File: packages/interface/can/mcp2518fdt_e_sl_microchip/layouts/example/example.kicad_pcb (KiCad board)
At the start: 2 copper layers, 6 parts

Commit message: Make package builds deterministic by wiring explicit local parts
The remaining packages now reference package-local concrete passives,
inductors, and other small parts directly instead of relying on generic
part-picker resolution. This aligns the source with the local
assets and removes the flaky live EasyEDA lookup path that was blocking
verification.

Constraint: Builds must not depend on unstable live part-picking when local package assets already exist
Constraint: Package-local parts remain the ownership boundary; no shared global part store was introduced
Rejected: Keep generic passives as the default style | repeated verification failures from upstream EasyEDA API instability
Rejected: Add ad hoc offline hacks around ato part-picking | weaker than making the package source deterministic
Confidence: high
Scope-risk: moderate
Reversibility: clean
Directive: For packages that already own generated local parts, instantiate those part modules directly and avoid generic passive declarations unless there is a strong reason not to
Tested:  passed for stm32g0b1kbu6_st, mcp2518fdt_e_sl_microchip, tcan3413ddfr_ti, raspberry_pi_hat_socket_zhouri, bq40z50rsmr_r2_4s_3a_ti, tps56637rpar_5v1_5a_ti, tps62933drlr_3v3_ti, bq25756rrvr_4s_2a_ti, tps2121ruxr_20v_4a_ti, and tps25730drefr_20v_3a_ti
Not-tested: Cross-package downstream integration beyond each package's default/example build
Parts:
- C1, C2: value 15pF ±5% -> (none)
- C3: value 1µF ±10% -> (none)
- C4: value 100nF ±10% -> (none)
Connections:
- net osc1_load-power-hv renamed can_ctrl-1
- net osc2_load-power-hv renamed 1
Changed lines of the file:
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@@
 	(net 7 "CLKO_SOF")
 	(net 8 "nINT")
-	(net 9 "osc1_load-power-hv")
+	(net 9 "can_ctrl-1")
 	(net 10 "8")
 	(net 11 "nINT0_GPIO0_XSTBY")
-	(net 12 "osc2_load-power-hv")
+	(net 12 "1")
 	(net 13 "lv")
 	(net 14 "hv")
@@
 			(size 0.57 2.04)
 			(layers "F.Cu" "F.Paste" "F.Mask")
-			(net 9 "osc1_load-power-hv")
+			(net 9 "can_ctrl-1")
 		)
 		(pad "5" smd oval
@@
 			(size 0.57 2.04)
 			(layers "F.Cu" "F.Paste" "F.Mask")
-			(net 12 "osc2_load-power-hv")
+			(net 12 "1")
 		)
 		(pad "4" smd oval
@@
 			(size 0.9 0.8)
 			(layers "F.Cu" "F.Paste" "F.Mask")
-			(net 12 "osc2_load-power-hv")
+			(net 12 "1")
 		)
 		(pad "4" smd rect
@@
 			(size 0.9 0.8)
 			(layers "F.Cu" "F.Paste" "F.Mask")
-			(net 9 "osc1_load-power-hv")
+			(net 9 "can_ctrl-1")
 		)
 		(embedded_fonts no)
@@
 			)
 		)
-		(property "Value" "15pF ±5%"
+		(property "Value" ""
 			(at 0 4)
 			(layer "F.Fab")
@@
 			(hide yes)
 		)
-		(property "Datasheet" "https://www.lcsc.com/datasheet/lcsc_datasheet_1810011652_Murata-Electronics-GRM1555C1H150JA01D_C76950.pdf"
+		(property "Datasheet" "https://www.lcsc.com/datasheet/lcsc_datasheet_1811081611_Murata-Electronics-GRM1555C1H150JA01D_C76950.pdf"
 			(at 0 0 0)
 			(layer "User.9")
@@
 			(size 0.5 0.54)
 			(layers "F.Cu" "F.Paste" "F.Mask")
-			(net 9 "osc1_load-power-hv")
+			(net 9 "can_ctrl-1")
 		)
 		(embedded_fonts no)
@@
 			)
 		)
-		(property "Value" "15pF ±5%"
+		(property "Value" ""
 			(at 0 4)
 			(layer "F.Fab")
@@
 			(hide yes)
 		)
-		(property "Datasheet" "https://www.lcsc.com/datasheet/lcsc_datasheet_1810011652_Murata-Electronics-GRM1555C1H150JA01D_C76950.pdf"
+		(property "Datasheet" "https://www.lcsc.com/datasheet/lcsc_datasheet_1811081611_Murata-Electronics-GRM1555C1H150JA01D_C76950.pdf"
 			(at 0 0 0)
 			(layer "User.9")
@@
 			(size 0.5 0.54)
 			(layers "F.Cu" "F.Paste" "F.Mask")
-			(net 12 "osc2_load-power-hv")
+			(net 12 "1")
 		)
 		(embedded_fonts no)
@@
 			)
 		)
-		(property "Value" "1µF ±10%"
+		(property "Value" ""
 			(at 0 4)
 			(layer "F.Fab")
@@
 			(hide yes)
 		)
-		(property "Datasheet" "https://www.lcsc.com/datasheet/lcsc_datasheet_1810011711_Murata-Electronics-GRM155R61C105KE01D_C77007.pdf"
+		(property "Datasheet" "https://wmsc.lcsc.com/wmsc/upload/file/pdf/v2/lcsc/1811081724_Murata-Electronics-GRM155R61C105KE01D_C77007.pdf"
 			(at 0 0 0)
 			(layer "User.9")
@@
 			)
 		)
-		(property "Value" "100nF ±10%"
+		(property "Value" ""
 			(at 0 4)
 			(layer "F.Fab")

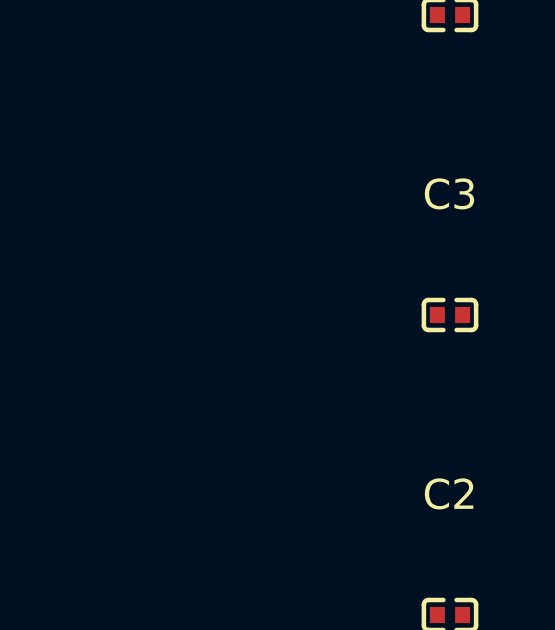
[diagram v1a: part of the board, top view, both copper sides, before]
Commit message: Make package schematics more readable and align passive choices with repo guidance
This pass improves the human-facing quality of the package library.
Explicit local capacitor/resistor parts now carry short descriptive
comments at the point of use, the MCP2518FD package swaps its 1uF bulk
capacitor to a 0603 part to match the current sizing rule, and several
packages add better net-name overrides for exposed and important internal
signals.

Constraint: Repo guidance now prefers explicit local parts and expects readable schematic net names
Constraint: Passive sizing should follow the current MLCC package rule unless a justified exception is needed
Rejected: Keep part instances comment-free | explicit local part names are not readable enough by themselves
Rejected: Leave the MCP2518FD 1uF bulk cap in 0402 | conflicts with the current 1uF-10uF 0603 guidance
Confidence: medium
Scope-risk: moderate
Reversibility: clean
Directive: When instantiating explicit local resistor/capacitor parts, include a short readable comment with the key value/package characteristics unless the name is already obviously human-readable
Tested:  passed for stm32g0b1kbu6_st, mcp2518fdt_e_sl_microchip, tcan3413ddfr_ti, raspberry_pi_hat_socket_zhouri, bq40z50rsmr_r2_4s_3a_ti, tps56637rpar_5v1_5a_ti, tps62933drlr_3v3_ti, bq25756rrvr_4s_2a_ti, tps2121ruxr_20v_4a_ti, and tps25730drefr_20v_3a_ti
Not-tested: Complete elimination of all internal autogenerated net labels in every package; some deep internal nets may still remain tool-driven
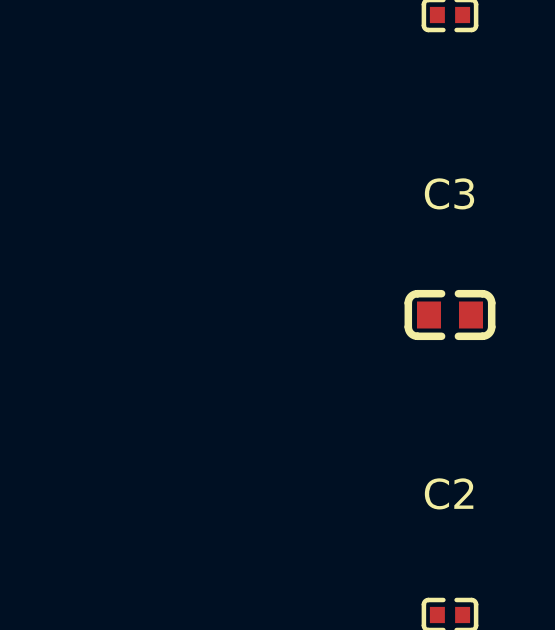
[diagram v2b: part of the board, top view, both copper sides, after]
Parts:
- C3: footprint Murata_Electronics_GRM155R61C105KE01D:C0402 -> Murata_Electronics_GRM188R61H105KAALD:C0603
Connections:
- net 1 renamed OSC2
- net 8 renamed nINT1_GPIO1
- net can_ctrl-1 renamed OSC1
- net hv renamed +3.3V
- net lv renamed GND
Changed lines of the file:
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@@
 	(net 7 "CLKO_SOF")
 	(net 8 "nINT")
-	(net 9 "can_ctrl-1")
-	(net 10 "8")
+	(net 9 "OSC1")
+	(net 10 "nINT1_GPIO1")
 	(net 11 "nINT0_GPIO0_XSTBY")
-	(net 12 "1")
-	(net 13 "lv")
-	(net 14 "hv")
+	(net 12 "OSC2")
+	(net 13 "GND")
+	(net 14 "+3.3V")
 	(footprint "Microchip_Tech_MCP2518FDT_E_SL:SOIC-14_L8.7-W3.9-P1.27-LS6.0-BL"
 		(layer "F.Cu")
@@
 			(size 0.57 2.04)
 			(layers "F.Cu" "F.Paste" "F.Mask")
-			(net 10 "8")
+			(net 10 "nINT1_GPIO1")
 		)
 		(pad "9" smd oval
@@
 			(size 0.57 2.04)
 			(layers "F.Cu" "F.Paste" "F.Mask")
-			(net 14 "hv")
+			(net 14 "+3.3V")
 		)
 		(pad "7" smd oval
@@
 			(size 0.57 2.04)
 			(layers "F.Cu" "F.Paste" "F.Mask")
-			(net 13 "lv")
+			(net 13 "GND")
 		)
 		(pad "6" smd oval
@@
 			(size 0.57 2.04)
 			(layers "F.Cu" "F.Paste" "F.Mask")
-			(net 9 "can_ctrl-1")
+			(net 9 "OSC1")
 		)
 		(pad "5" smd oval
@@
 			(size 0.57 2.04)
 			(layers "F.Cu" "F.Paste" "F.Mask")
-			(net 12 "1")
+			(net 12 "OSC2")
 		)
 		(pad "4" smd oval
@@
 			(size 0.9 0.8)
 			(layers "F.Cu" "F.Paste" "F.Mask")
-			(net 13 "lv")
+			(net 13 "GND")
 		)
 		(pad "3" smd rect
@@
 			(size 0.9 0.8)
 			(layers "F.Cu" "F.Paste" "F.Mask")
-			(net 12 "1")
+			(net 12 "OSC2")
 		)
 		(pad "4" smd rect
@@
 			(size 0.9 0.8)
 			(layers "F.Cu" "F.Paste" "F.Mask")
-			(net 13 "lv")
+			(net 13 "GND")
 		)
 		(pad "1" smd rect
@@
 			(size 0.9 0.8)
 			(layers "F.Cu" "F.Paste" "F.Mask")
-			(net 9 "can_ctrl-1")
+			(net 9 "OSC1")
 		)
 		(embedded_fonts no)
@@
 			(size 0.5 0.54)
 			(layers "F.Cu" "F.Paste" "F.Mask")
-			(net 13 "lv")
+			(net 13 "GND")
 		)
 		(pad "1" smd rect
@@
 			(size 0.5 0.54)
 			(layers "F.Cu" "F.Paste" "F.Mask")
-			(net 9 "can_ctrl-1")
+			(net 9 "OSC1")
 		)
 		(embedded_fonts no)
@@
 			(size 0.5 0.54)
 			(layers "F.Cu" "F.Paste" "F.Mask")
-			(net 13 "lv")
+			(net 13 "GND")
 		)
 		(pad "1" smd rect
@@
 			(size 0.5 0.54)
 			(layers "F.Cu" "F.Paste" "F.Mask")
-			(net 12 "1")
+			(net 12 "OSC2")
 		)
 		(embedded_fonts no)
@@
 		)
 	)
-	(footprint "Murata_Electronics_GRM155R61C105KE01D:C0402"
+	(footprint "Murata_Electronics_GRM188R61H105KAALD:C0603"
 		(layer "F.Cu")
 		(at 20 -20 0)
@@
 			)
 		)
-		(property "LCSC" "C77007"
+		(property "LCSC" "C77386"
 			(at 0 0 0)
 			(layer "User.9")
@@
 			(hide yes)
 		)
-		(property "Partnumber" "GRM155R61C105KE01D"
-			(at 0 0 0)
-			(layer "User.9")
-			(hide yes)
-		)
-		(property "Datasheet" "https://wmsc.lcsc.com/wmsc/upload/file/pdf/v2/lcsc/1811081724_Murata-Electronics-GRM155R61C105KE01D_C77007.pdf"
+		(property "Partnumber" "GRM188R61H105KAALD"
+			(at 0 0 0)
+			(layer "User.9")
+			(hide yes)
+		)
+		(property "Datasheet" "https://wmsc.lcsc.com/wmsc/upload/file/pdf/v2/lcsc/1811012005_Murata-Electronics-GRM188R61H105KAALD_C77386.pdf"
 			(at 0 0 0)
 			(layer "User.9")
@@
 			(hide yes)
 		)
-		(property "lcsc_id" "C77007"
+		(property "lcsc_id" "C77386"
 			(at 0 0 0)
 			(layer "User.9")
@@
 		(attr smd)
 		(fp_line
-			(start -0.72 -0.5)
-			(end -0.22 -0.5)
-			(stroke
-				(width 0.15)
-				(type solid)
-			)
-			(layer "F.SilkS")
-			(layers "F.SilkS")
-			(locked no)
-		)
-		(fp_line
-			(start -0.87 0.35)
-			(end -0.87 -0.35)
-			(stroke
-				(width 0.15)
-				(type solid)
-			)
-			(layer "F.SilkS")
-			(layers "F.SilkS")
-			(locked no)
-		)
-		(fp_line
-			(start -0.22 0.5)
-			(end -0.72 0.5)
-			(stroke
-				(width 0.15)
-				(type solid)
-			)
-			(layer "F.SilkS")
-			(layers "F.SilkS")
-			(locked no)
-		)
-		(fp_line
-			(start 0.72 0.5)
-			(end 0.22 0.5)
-			(stroke
-				(width 0.15)
-				(type solid)
-			)
-			(layer "F.SilkS")
-			(layers "F.SilkS")
-			(locked no)
-		)
-		(fp_line
-			(start 0.22 -0.5)
-			(end 0.72 -0.5)
-			(stroke
-				(width 0.15)
-				(type solid)
-			)
-			(layer "F.SilkS")
-			(layers "F.SilkS")
-			(locked no)
-		)
-		(fp_line
-			(start 0.87 -0.35)
-			(end 0.87 0.35)
-			(stroke
-				(width 0.15)
-				(type solid)
-			)
-			(layer "F.SilkS")
-			(layers "F.SilkS")
-			(locked no)
-		)
-		(fp_arc
-			(start 0.87 -0.35)
-			(mid 0.826066 -0.456066)
-			(end 0.72 -0.5)
-			(stroke
-				(width 0.15)
-				(type solid)
-			)
-			(layer "F.SilkS")
-			(locked no)
-		)
-		(fp_arc
-			(start 0.72 0.5)
-			(mid 0.826066 0.456066)
-			(end 0.87 0.35)
-			(stroke
-				(width 0.15)
-				(type solid)
-			)
-			(layer "F.SilkS")
-			(locked no)
-		)
-		(fp_arc
-			(start -0.87 0.35)
-			(mid -0.826066 0.456066)
-			(end -0.72 0.5)
-			(stroke
-				(width 0.15)
-				(type solid)
-			)
-			(layer "F.SilkS")
-			(locked no)
-		)
-		(fp_arc
-			(start -0.72 -0.5)
-			(mid -0.826066 -0.456066)
-			(end -0.87 -0.35)
-			(stroke
-				(width 0.15)
+			(start -0.28 0.71)
+			(end -1.08 0.71)
+			(stroke
+				(width 0.25)
+				(type solid)
+			)
+			(layer "F.SilkS")
+			(layers "F.SilkS")
+			(locked no)
+		)
+		(fp_line
+			(start 0.28 0.71)
+			(end 1.08 0.71)
+			(stroke
+				(width 0.25)
+				(type solid)
+			)
+			(layer "F.SilkS")
+			(layers "F.SilkS")
+			(locked no)
+		)
+		(fp_line
+			(start -0.28 -0.71)
+			(end -1.08 -0.71)
+			(stroke
+				(width 0.25)
+				(type solid)
+			)
+			(layer "F.SilkS")
+			(layers "F.SilkS")
+			(locked no)
+		)
+		(fp_line
+			(start 0.28 -0.71)
+			(end 1.08 -0.71)
+			(stroke
+				(width 0.25)
+				(type solid)
+			)
+			(layer "F.SilkS")
+			(layers "F.SilkS")
+			(locked no)
+		)
+		(fp_line
+			(start -1.39 0.4)
+			(end -1.39 -0.4)
+			(stroke
+				(width 0.25)
+				(type solid)
+			)
+			(layer "F.SilkS")
+			(layers "F.SilkS")
+			(locked no)
+		)
+		(fp_line
+			(start 1.39 -0.4)
+			(end 1.39 0.4)
+			(stroke
+				(width 0.25)
+				(type solid)
+			)
+			(layer "F.SilkS")
+			(layers "F.SilkS")
+			(locked no)
+		)
+		(fp_arc
+			(start 1.39 -0.4)
+			(mid 1.2992031 -0.6192031)
+			(end 1.08 -0.71)
+			(stroke
+				(width 0.25)
+				(type solid)
+			)
+			(layer "F.SilkS")
+			(locked no)
+		)
+		(fp_arc
+			(start 1.08 0.71)
+			(mid 1.2992031 0.6192031)
+			(end 1.39 0.4)
+			(stroke
+				(width 0.25)
+				(type solid)
+			)
+			(layer "F.SilkS")
+			(locked no)
+		)
+		(fp_arc
+			(start -1.39 0.4)
+			(mid -1.2992031 0.6192031)
+			(end -1.08 0.71)
+			(stroke
+				(width 0.25)
+				(type solid)
+			)
+			(layer "F.SilkS")
+			(locked no)
+		)
+		(fp_arc
+			(start -1.08 -0.71)
+			(mid -1.2992031 -0.6192031)
+			(end -1.39 -0.4)
+			(stroke
+				(width 0.25)
 				(type solid)
 			)
@@
 		)
 		(fp_circle
-			(center -0.5 0.25)
-			(end -0.47 0.25)
+			(center -0.8 0.4)
+			(end -0.77 0.4)
 			(stroke
 				(width 0.06)
@@
 		)
 		(pad "2" smd rect
-			(at 0.42 0 0)
-			(size 0.5 0.54)
-			(layers "F.Cu" "F.Paste" "F.Mask")
-			(net 13 "lv")
+			(at 0.7 0 0)
+			(size 0.8 0.9)
+			(layers "F.Cu" "F.Paste" "F.Mask")
+			(net 13 "GND")
 		)
 		(pad "1" smd rect
-			(at -0.42 0 0)
-			(size 0.5 0.54)
-			(layers "F.Cu" "F.Paste" "F.Mask")
-			(net 14 "hv")
+			(at -0.7 0 0)
+			(size 0.8 0.9)
+			(layers "F.Cu" "F.Paste" "F.Mask")
+			(net 14 "+3.3V")
 		)
 		(embedded_fonts no)
-		(model "${KIPRJMOD}/../../parts/Murata_Electronics_GRM155R61C105KE01D/C0402_L1.0-W0.5-H0.5.step"
+		(model "${KIPRJMOD}/../../parts/Murata_Electronics_GRM188R61H105KAALD/C0603_L1.6-W0.8-H0.8.step"
 			(offset
 				(xyz 0 0 -0)
@@
 			(size 0.5 0.54)
 			(layers "F.Cu" "F.Paste" "F.Mask")
-			(net 13 "lv")
+			(net 13 "GND")
 		)
 		(pad "1" smd rect
@@
 			(size 0.5 0.54)
 			(layers "F.Cu" "F.Paste" "F.Mask")
-			(net 14 "hv")
+			(net 14 "+3.3V")
 		)
 		(embedded_fonts no)

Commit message: Finish removing net-name overrides from reusable packages
This completes the package-level override cleanup by deleting the remaining
`override_net_name` assignments from the library's reusable package modules and
rebuilding their checked-in layouts so generated net metadata matches source.
The package interfaces stay the same; only the forced net naming was removed so
these modules compose cleanly when imported into downstream designs.

Constraint: The library must stay reusable and avoid imposed internal net names leaking into consuming designs
Constraint: Each changed package must still verify with the repo's Atopile workflow after layout regeneration
Rejected: Stop after the battery frontend cleanup | leaves the same composition hazard in other packages
Rejected: Remove override lines without rebuilding layouts | would leave stale generated PCB net names checked into the repo
Confidence: high
Scope-risk: moderate
Reversibility: clean
Directive: Do not reintroduce `override_net_name` in reusable package modules unless a package is intentionally design-specific
Tested: `uv tool run --from atopile==0.15.4 ato --non-interactive build` in each affected package directory (stm32g0b1kbu6_st, mcp2518fdt_e_sl_microchip, tcan3413ddfr_ti, raspberry_pi_hat_socket_zhouri, tps56637rpar_5v1_5a_ti, tps62933drlr_3v3_ti, bq25756rrvr_4s_2a_ti, tps2121ruxr_20v_4a_ti, tps25730drefr_20v_3a_ti)
Not-tested: Downstream consumer projects that may have been depending on the old forced net names in generated layouts
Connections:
- net +3.3V renamed hv
- net GND renamed lv
- net OSC1 renamed can_ctrl-1
- net OSC2 renamed 1
- net nINT1_GPIO1 renamed 8
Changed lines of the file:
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@@
 	(net 7 "CLKO_SOF")
 	(net 8 "nINT")
-	(net 9 "OSC1")
-	(net 10 "nINT1_GPIO1")
+	(net 9 "can_ctrl-1")
+	(net 10 "8")
 	(net 11 "nINT0_GPIO0_XSTBY")
-	(net 12 "OSC2")
-	(net 13 "GND")
-	(net 14 "+3.3V")
+	(net 12 "1")
+	(net 13 "lv")
+	(net 14 "hv")
 	(footprint "Microchip_Tech_MCP2518FDT_E_SL:SOIC-14_L8.7-W3.9-P1.27-LS6.0-BL"
 		(layer "F.Cu")
@@
 			(size 0.57 2.04)
 			(layers "F.Cu" "F.Paste" "F.Mask")
-			(net 10 "nINT1_GPIO1")
+			(net 10 "8")
 		)
 		(pad "9" smd oval
@@
 			(size 0.57 2.04)
 			(layers "F.Cu" "F.Paste" "F.Mask")
-			(net 14 "+3.3V")
+			(net 14 "hv")
 		)
 		(pad "7" smd oval
@@
 			(size 0.57 2.04)
 			(layers "F.Cu" "F.Paste" "F.Mask")
-			(net 13 "GND")
+			(net 13 "lv")
 		)
 		(pad "6" smd oval
@@
 			(size 0.57 2.04)
 			(layers "F.Cu" "F.Paste" "F.Mask")
-			(net 9 "OSC1")
+			(net 9 "can_ctrl-1")
 		)
 		(pad "5" smd oval
@@
 			(size 0.57 2.04)
 			(layers "F.Cu" "F.Paste" "F.Mask")
-			(net 12 "OSC2")
+			(net 12 "1")
 		)
 		(pad "4" smd oval
@@
 			(size 0.9 0.8)
 			(layers "F.Cu" "F.Paste" "F.Mask")
-			(net 13 "GND")
+			(net 13 "lv")
 		)
 		(pad "3" smd rect
@@
 			(size 0.9 0.8)
 			(layers "F.Cu" "F.Paste" "F.Mask")
-			(net 12 "OSC2")
+			(net 12 "1")
 		)
 		(pad "4" smd rect
@@
 			(size 0.9 0.8)
 			(layers "F.Cu" "F.Paste" "F.Mask")
-			(net 13 "GND")
+			(net 13 "lv")
 		)
 		(pad "1" smd rect
@@
 			(size 0.9 0.8)
 			(layers "F.Cu" "F.Paste" "F.Mask")
-			(net 9 "OSC1")
+			(net 9 "can_ctrl-1")
 		)
 		(embedded_fonts no)
@@
 			(size 0.5 0.54)
 			(layers "F.Cu" "F.Paste" "F.Mask")
-			(net 13 "GND")
+			(net 13 "lv")
 		)
 		(pad "1" smd rect
@@
 			(size 0.5 0.54)
 			(layers "F.Cu" "F.Paste" "F.Mask")
-			(net 9 "OSC1")
+			(net 9 "can_ctrl-1")
 		)
 		(embedded_fonts no)
@@
 			(size 0.5 0.54)
 			(layers "F.Cu" "F.Paste" "F.Mask")
-			(net 13 "GND")
+			(net 13 "lv")
 		)
 		(pad "1" smd rect
@@
 			(size 0.5 0.54)
 			(layers "F.Cu" "F.Paste" "F.Mask")
-			(net 12 "OSC2")
+			(net 12 "1")
 		)
 		(embedded_fonts no)
@@
 			(size 0.8 0.9)
 			(layers "F.Cu" "F.Paste" "F.Mask")
-			(net 13 "GND")
+			(net 13 "lv")
 		)
 		(pad "1" smd rect
@@
 			(size 0.8 0.9)
 			(layers "F.Cu" "F.Paste" "F.Mask")
-			(net 14 "+3.3V")
+			(net 14 "hv")
 		)
 		(embedded_fonts no)
@@
 			(size 0.5 0.54)
 			(layers "F.Cu" "F.Paste" "F.Mask")
-			(net 13 "GND")
+			(net 13 "lv")
 		)
 		(pad "1" smd rect
@@
 			(size 0.5 0.54)
 			(layers "F.Cu" "F.Paste" "F.Mask")
-			(net 14 "+3.3V")
+			(net 14 "hv")
 		)
 		(embedded_fonts no)
